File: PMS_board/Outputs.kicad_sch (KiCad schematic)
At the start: 37 parts, among them U1 VN7140ASTR, U11 VN7007AHTR, U2 VN7140ASTR, U23 VN7007AHTR, U8 VN7140ASTR

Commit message: How did our footprints get this geeked???
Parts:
- C54, C59: footprint Capacitor_SMD:C_0603_1608Metric -> Capacitor_SMD:C_0603_1608Metric_Pad1.08x0.95mm_HandSolder
- D11, D13, D21, D6, D7: footprint LED_SMD:LED_Cree-XHP50_3V_HighDensity -> (none)
- D12, D20, D22: footprint Diode_SMD:Littelfuse_PolyZen-LS -> (none)
- R16, R17, R18, R19, R20, R67, R68, R69, R70, R71, R72, R73, R74, R75, R76, R77, R78, R79, R80, R81, R82, R83: footprint (none) -> Resistor_SMD:R_0603_1608Metric_Pad0.98x0.95mm_HandSolder
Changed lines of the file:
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@@
 			)
 		)
-		(property "Footprint" ""
+		(property "Footprint" "Resistor_SMD:R_0603_1608Metric_Pad0.98x0.95mm_HandSolder"
 			(at 54.864 126.746 90)
 			(hide yes)
@@
 			)
 		)
-		(property "Footprint" ""
+		(property "Footprint" "Resistor_SMD:R_0603_1608Metric_Pad0.98x0.95mm_HandSolder"
 			(at 106.934 46.736 90)
 			(hide yes)
@@
 			)
 		)
-		(property "Footprint" "LED_SMD:LED_Cree-XHP50_3V_HighDensity"
+		(property "Footprint" ""
 			(at 111.76 40.64 0)
 			(hide yes)
@@
 			)
 		)
-		(property "Footprint" ""
+		(property "Footprint" "Resistor_SMD:R_0603_1608Metric_Pad0.98x0.95mm_HandSolder"
 			(at 50.546 102.616 90)
 			(hide yes)
@@
 			)
 		)
-		(property "Footprint" ""
+		(property "Footprint" "Resistor_SMD:R_0603_1608Metric_Pad0.98x0.95mm_HandSolder"
 			(at 112.014 143.256 90)
 			(hide yes)
@@
 			)
 		)
-		(property "Footprint" "Capacitor_SMD:C_0603_1608Metric"
+		(property "Footprint" "Capacitor_SMD:C_0603_1608Metric_Pad1.08x0.95mm_HandSolder"
 			(at 29.5148 57.15 0)
 			(hide yes)
@@
 			)
 		)
-		(property "Footprint" ""
+		(property "Footprint" "Resistor_SMD:R_0603_1608Metric_Pad0.98x0.95mm_HandSolder"
 			(at 54.864 91.186 90)
 			(hide yes)
@@
 			)
 		)
-		(property "Footprint" ""
+		(property "Footprint" "Resistor_SMD:R_0603_1608Metric_Pad0.98x0.95mm_HandSolder"
 			(at 112.014 107.696 90)
 			(hide yes)
@@
 			)
 		)
-		(property "Footprint" ""
+		(property "Footprint" "Resistor_SMD:R_0603_1608Metric_Pad0.98x0.95mm_HandSolder"
 			(at 50.546 173.736 90)
 			(hide yes)
@@
 			)
 		)
-		(property "Footprint" ""
+		(property "Footprint" "Resistor_SMD:R_0603_1608Metric_Pad0.98x0.95mm_HandSolder"
 			(at 50.546 138.176 90)
 			(hide yes)
@@
 			)
 		)
-		(property "Footprint" ""
+		(property "Footprint" "Resistor_SMD:R_0603_1608Metric_Pad0.98x0.95mm_HandSolder"
 			(at 54.864 162.306 90)
 			(hide yes)
@@
 			)
 		)
-		(property "Footprint" "LED_SMD:LED_Cree-XHP50_3V_HighDensity"
+		(property "Footprint" ""
 			(at 116.84 173.99 0)
 			(hide yes)
@@
 			)
 		)
-		(property "Footprint" "LED_SMD:LED_Cree-XHP50_3V_HighDensity"
+		(property "Footprint" ""
 			(at 111.76 67.31 0)
 			(hide yes)
@@
 			)
 		)
-		(property "Footprint" ""
+		(property "Footprint" "Resistor_SMD:R_0603_1608Metric_Pad0.98x0.95mm_HandSolder"
 			(at 36.576 54.864 90)
 			(hide yes)
@@
 			)
 		)
-		(property "Footprint" ""
+		(property "Footprint" "Resistor_SMD:R_0603_1608Metric_Pad0.98x0.95mm_HandSolder"
 			(at 42.164 34.544 90)
 			(hide yes)
@@
 			)
 		)
-		(property "Footprint" ""
+		(property "Footprint" "Resistor_SMD:R_0603_1608Metric_Pad0.98x0.95mm_HandSolder"
 			(at 110.744 30.226 90)
 			(hide yes)
@@
 			)
 		)
-		(property "Footprint" ""
+		(property "Footprint" "Resistor_SMD:R_0603_1608Metric_Pad0.98x0.95mm_HandSolder"
 			(at 54.864 98.806 90)
 			(hide yes)
@@
 			)
 		)
-		(property "Footprint" ""
+		(property "Footprint" "Resistor_SMD:R_0603_1608Metric_Pad0.98x0.95mm_HandSolder"
 			(at 54.864 134.366 90)
 			(hide yes)
@@
 			)
 		)
-		(property "Footprint" "LED_SMD:LED_Cree-XHP50_3V_HighDensity"
+		(property "Footprint" ""
 			(at 116.84 102.87 0)
 			(hide yes)
@@
 			)
 		)
-		(property "Footprint" ""
+		(property "Footprint" "Resistor_SMD:R_0603_1608Metric_Pad0.98x0.95mm_HandSolder"
 			(at 60.706 30.734 90)
 			(hide yes)
@@
 			)
 		)
-		(property "Footprint" ""
+		(property "Footprint" "Resistor_SMD:R_0603_1608Metric_Pad0.98x0.95mm_HandSolder"
 			(at 110.744 56.896 90)
 			(hide yes)
@@
 			)
 		)
-		(property "Footprint" ""
+		(property "Footprint" "Resistor_SMD:R_0603_1608Metric_Pad0.98x0.95mm_HandSolder"
 			(at 106.934 73.406 90)
 			(hide yes)
@@
 			)
 		)
-		(property "Footprint" ""
+		(property "Footprint" "Resistor_SMD:R_0603_1608Metric_Pad0.98x0.95mm_HandSolder"
 			(at 60.706 57.404 90)
 			(hide yes)
@@
 			)
 		)
-		(property "Footprint" "Diode_SMD:Littelfuse_PolyZen-LS"
+		(property "Footprint" ""
 			(at 45.72 138.43 0)
 			(hide yes)
@@
 			)
 		)
-		(property "Footprint" ""
+		(property "Footprint" "Resistor_SMD:R_0603_1608Metric_Pad0.98x0.95mm_HandSolder"
 			(at 36.576 28.194 90)
 			(hide yes)
@@
 			)
 		)
-		(property "Footprint" "Capacitor_SMD:C_0603_1608Metric"
+		(property "Footprint" "Capacitor_SMD:C_0603_1608Metric_Pad1.08x0.95mm_HandSolder"
 			(at 29.5148 30.48 0)
 			(hide yes)
@@
 			)
 		)
-		(property "Footprint" ""
+		(property "Footprint" "Resistor_SMD:R_0603_1608Metric_Pad0.98x0.95mm_HandSolder"
 			(at 54.864 169.926 90)
 			(hide yes)
@@
 			)
 		)
-		(property "Footprint" ""
+		(property "Footprint" "Resistor_SMD:R_0603_1608Metric_Pad0.98x0.95mm_HandSolder"
 			(at 42.164 61.214 90)
 			(hide yes)
@@
 			)
 		)
-		(property "Footprint" ""
+		(property "Footprint" "Resistor_SMD:R_0603_1608Metric_Pad0.98x0.95mm_HandSolder"
 			(at 112.014 178.816 90)
 			(hide yes)
@@
 			)
 		)
-		(property "Footprint" "Diode_SMD:Littelfuse_PolyZen-LS"
+		(property "Footprint" ""
 			(at 45.72 102.87 0)
 			(hide yes)
@@
 			)
 		)
-		(property "Footprint" "Diode_SMD:Littelfuse_PolyZen-LS"
+		(property "Footprint" ""
 			(at 45.72 173.99 0)
 			(hide yes)
@@
 			)
 		)
-		(property "Footprint" "LED_SMD:LED_Cree-XHP50_3V_HighDensity"
+		(property "Footprint" ""
 			(at 116.84 138.43 0)
 			(hide yes)

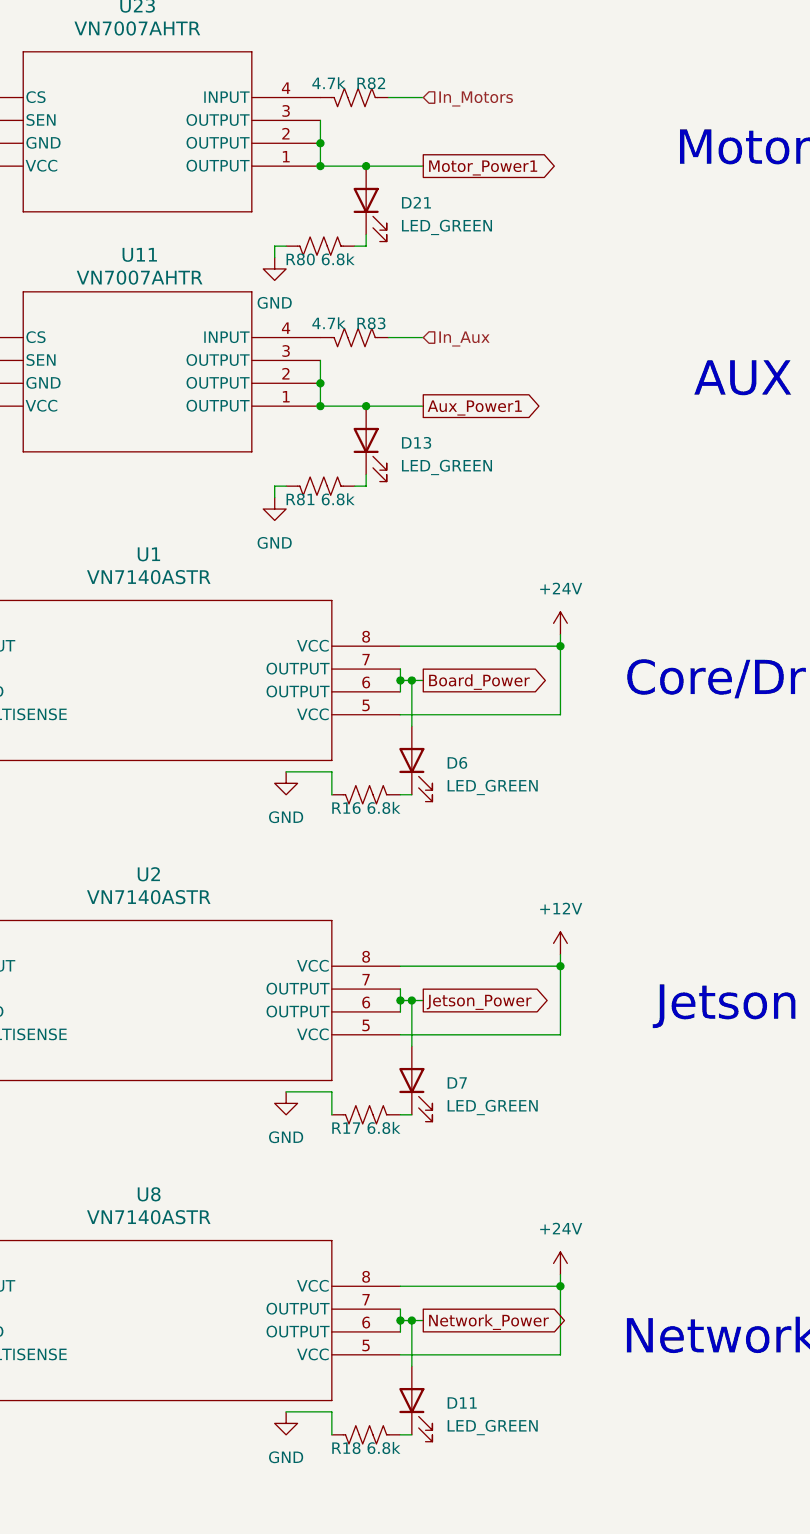
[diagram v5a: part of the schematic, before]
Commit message: Footprints and naming things
Changed component names to be a bit more representitive

Some minor footprints
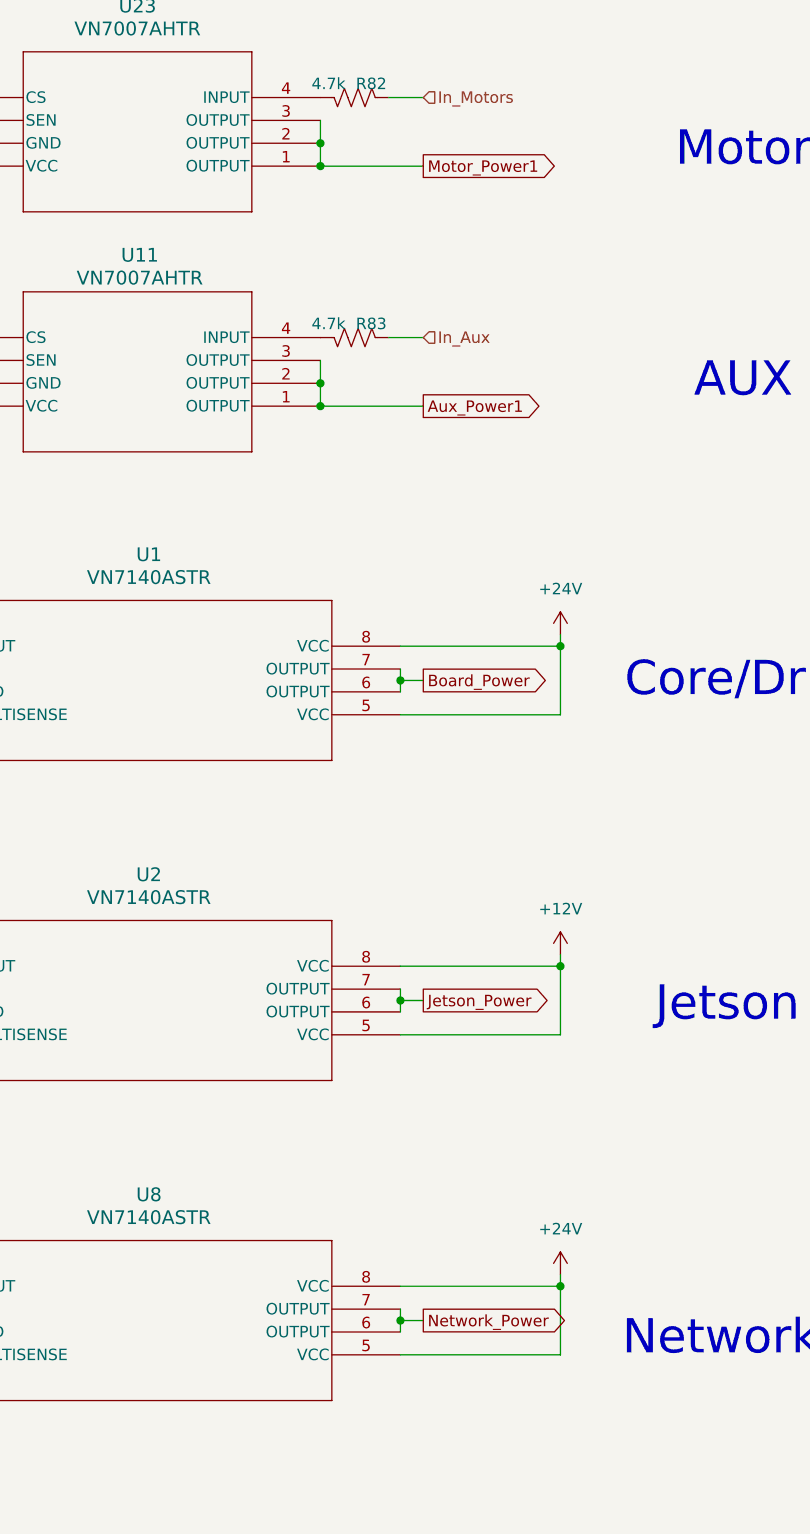
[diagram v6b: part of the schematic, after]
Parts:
- removed D11, D13, D21, D6, D7: LED_GREEN, symbol Device:LED
- removed R16, R17, R18, R80, R81: 6.8k, Resistor_SMD:R_0603_1608Metric_Pad0.98x0.95mm_HandSolder, symbol Device:R_US

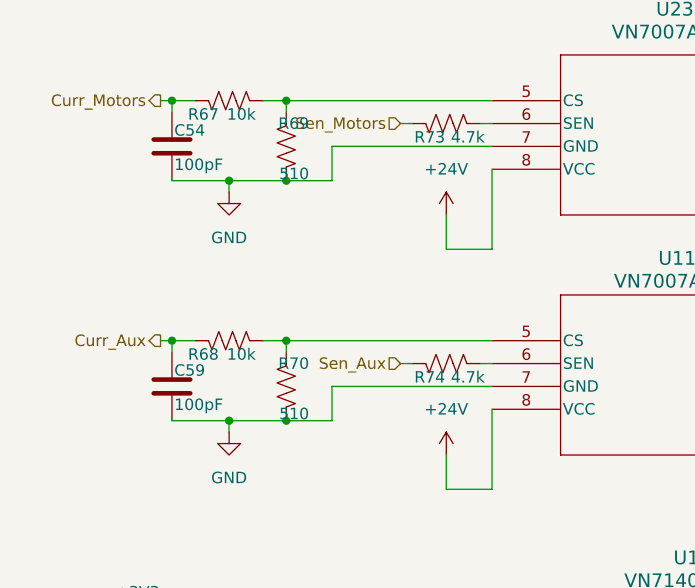
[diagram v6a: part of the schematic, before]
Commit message: New resistor values and more footprints
LED footprints
Changed resistor values as Drew requested
Op amp datasheets and footprints
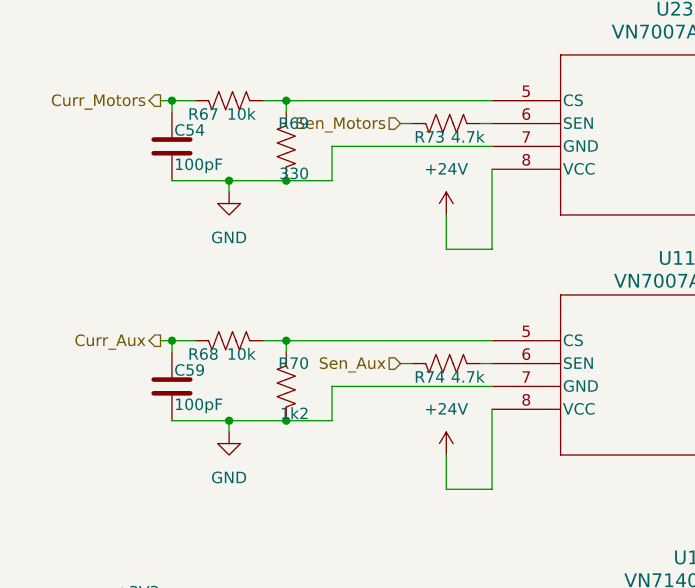
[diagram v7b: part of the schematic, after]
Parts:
- R69: value 510 -> 330
- R70: value 510 -> 1k2
